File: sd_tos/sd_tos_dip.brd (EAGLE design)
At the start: 19.5 x 63.5 mm, 20 parts, among them IC1 MEGA16-A, IC3 74HCT595D

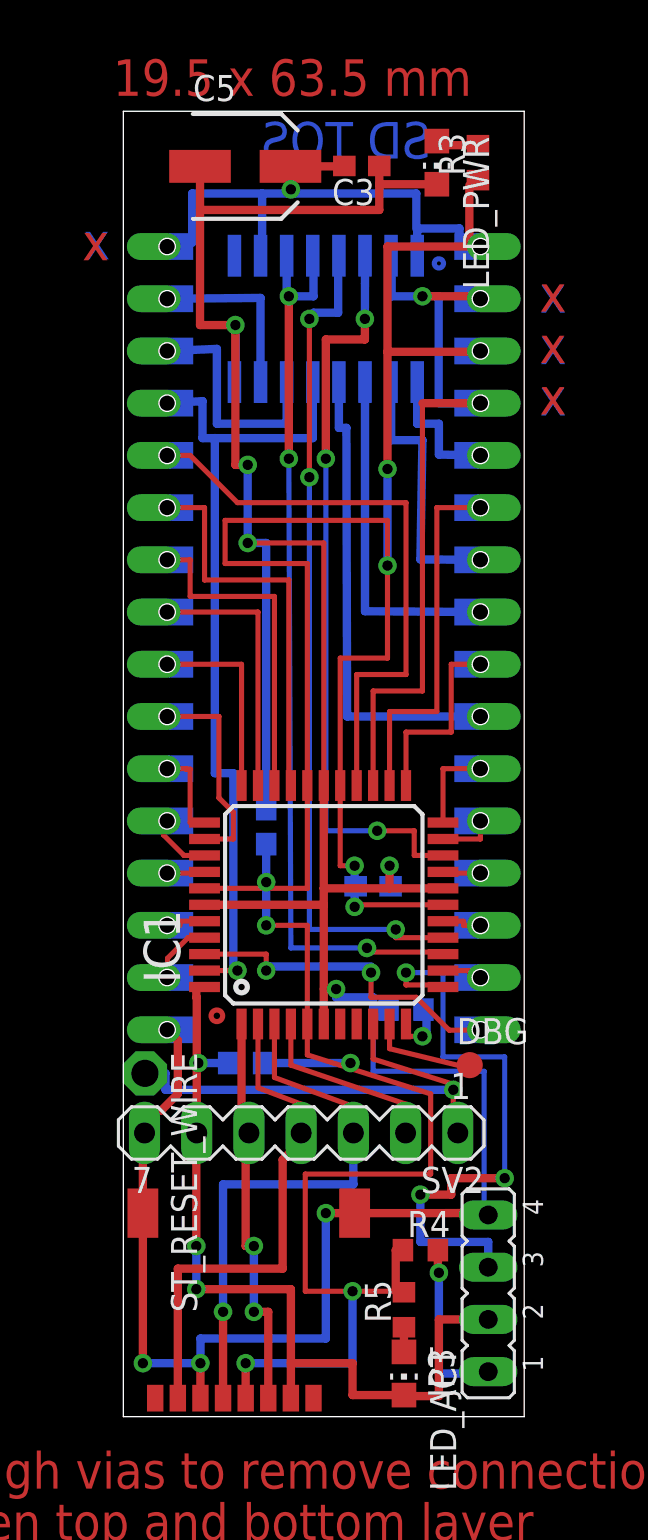
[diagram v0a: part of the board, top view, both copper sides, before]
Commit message: lines now thicker for easier pcb making
git-svn-id: https://subversion.assembla.com/svn/atarijookie/trunk@938 0d2ca917-fb58-4453-bb26-a698c01b0940
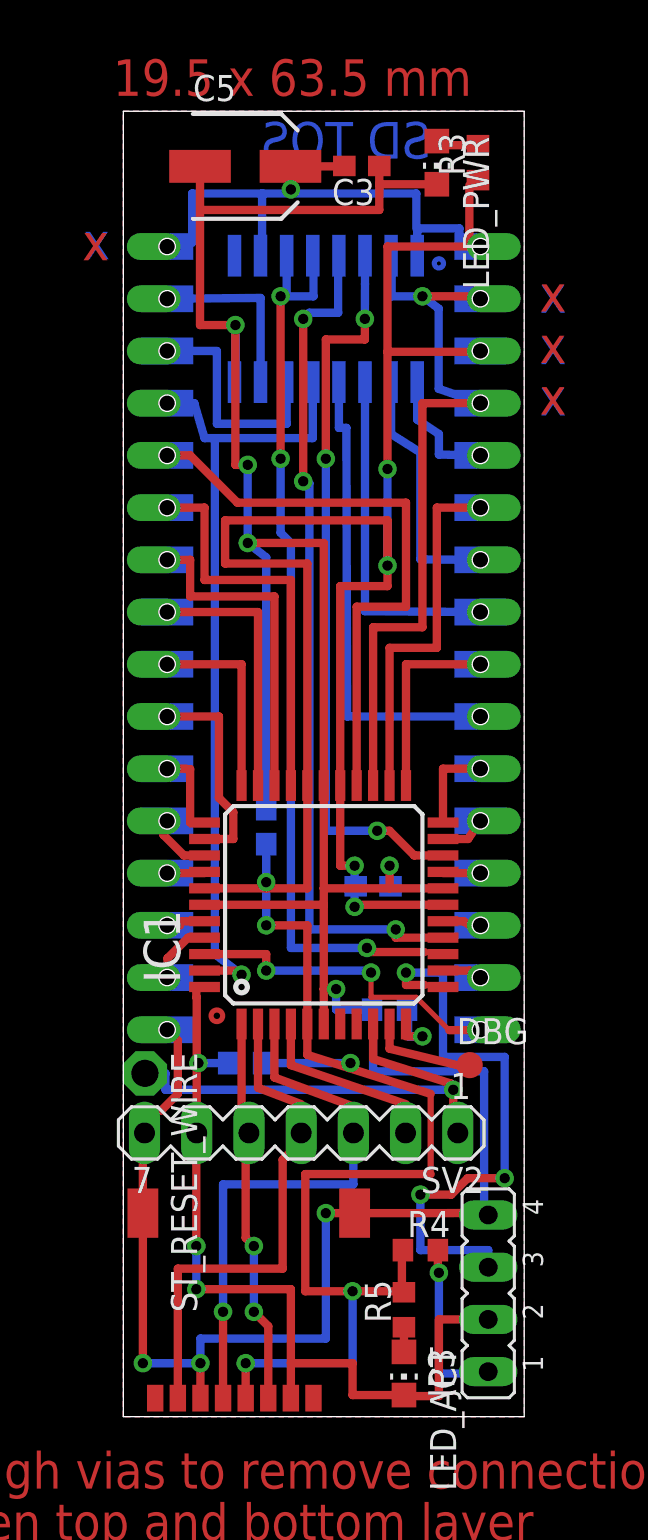
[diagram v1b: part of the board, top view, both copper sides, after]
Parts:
- moved R2 0.80 mm to (47.7, 23.8)
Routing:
- net GND: track 157.5 -> 156.3 mm
- net A14: track 14.5 -> 13.5 mm
- net A9: track 13.1 -> 12.3 mm
- net SIPO_D: track 36.8 -> 36.1 mm
- net SIPO_CLK: track 44.7 -> 45.4 mm
- net MOSI: track 19.7 -> 19.0 mm
- net SIPO_OE: track 41.0 -> 41.5 mm
- net BTN: track 30.0 -> 29.5 mm
- added copper zone on layer 1, net GND
- added copper zone on layer 16, net GND
